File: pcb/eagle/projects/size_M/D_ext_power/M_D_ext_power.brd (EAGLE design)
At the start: 21 parts

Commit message: PCB M.1
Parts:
- added D.F1, D.F2: (no value), rcl:R0805
- added D.R2, D.R5: 5k1, rcl:R0603
- added D.R9: TERM_10K, hugo:THERM
- D.R3: value 12k -> 1k
- D.U1: value MCP -> MCP73833-AMI_UN; device !stavebnice03:SOT23-5 -> SamacSys_Parts:SOP50P490X110-10N
- D.U2: value TC -> LM3671_3.3
- moved D.U1 1.03 mm to (6.10, 13.7), turned to 0 degrees
- moved D.C7 0.59 mm to (9.74, 17.1)
- moved D.C6 0.54 mm to (5.21, 16.8), flipped to the top
- moved D.R7 0.18 mm to (14.7, 9.93)
- moved D.R4 0.14 mm to (8.43, 7.32)
- moved D.C4 0.09 mm to (8.39, 10.0)
- renumbered D.IC2 to D.U3
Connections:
- removed net N$11: D.R3.2, D.U1.5
- removed net N$12: D.J3.2, D.R7.1, D.T1.S, D.U2.VIN
- removed net N$13: D.C6.2, D.LIPOL.2, D.R8.2, D.U1.3, D.U3.7
- removed net N$8: D.R8.1, D.T1.D, D.U3.8
- removed net N$9: D.C4.2, D.J3.1, D.R4.2, D.T1.G, D.U1.4, U$1.A4B9, U$1.B4A9
- removed net VDD: D.C1.2, D.C7.2, D.D1.2, D.J3.3, D.L1.2, D.R1.1, D.U2.BP, D.U3.5
- new net 3V3F: D.F1.2, D.J3.3
- new net IN+: D.C6.2, D.LIPOL.2, D.R8.2, D.U1.10, D.U1.9, D.U3.8
- new net IN-: D.R8.1, D.T1.D, D.U3.7
- new net N$10: D.R9.2, D.U1.8
- new net N$4: D.R5.1, U$1.B5
- new net N$6: D.R2.1, U$1.A5
- new net N$7: D.R3.2, D.U1.6
- new net VBATF: D.F2.2, D.J3.2
- new net VCC: D.C1.2, D.C7.2, D.D1.2, D.F1.1, D.L1.2, D.R1.1, D.U2.BP, D.U3.5
- new net VMOT: D.F2.1, D.R7.1, D.T1.S, D.U2.VIN
- new net VUSB: D.C4.2, D.J3.1, D.R4.2, D.T1.G, D.U1.1, D.U1.2, U$1.A4B9, U$1.B4A9
- net GND: now also D.R2.2, D.R5.2, D.R9.1, D.U1.5; no longer D.U1.2
- net P4: now also D.U1.3; no longer D.U1.1
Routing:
- net VUSB: track 0.00 -> 35.7 mm, vias 0 -> 1
- net VDD: track 34.2 -> 0.00 mm, vias 1 -> 0
- net N$9: track 33.0 -> 0.00 mm, vias 1 -> 0
- net VCC: track 0.00 -> 30.9 mm, vias 0 -> 1
- net GND: track 99.6 -> 122.1 mm, vias 4 -> 6
- net N$13: track 16.0 -> 0.00 mm, vias 1 -> 0
- net N$12: track 14.8 -> 0.00 mm, vias 1 -> 0
- net IN+: track 0.00 -> 14.8 mm, vias 0 -> 2
- net VMOT: track 0.00 -> 14.6 mm, vias 0 -> 1
- net N$10: track 0.00 -> 13.7 mm, vias 0 -> 1
- net N$8: track 9.31 -> 0.00 mm, vias 1 -> 0
- net IN-: track 0.00 -> 8.86 mm, vias 0 -> 1
- net P4: track 14.6 -> 21.8 mm
- net 3V3F: track 0.00 -> 3.66 mm
- net VBATF: track 0.00 -> 3.21 mm
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- added copper zone on layer 16, net IN+
- added copper zone on layer 16, net VUSB

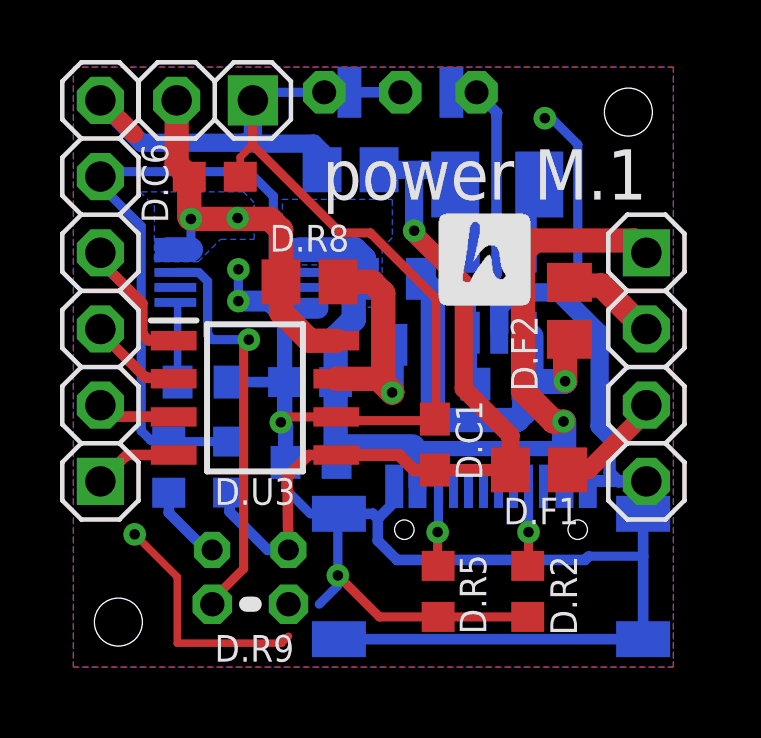
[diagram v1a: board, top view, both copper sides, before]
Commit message: repository structure reorganized (tiny-blocks moved to a separate directory) implemented tiny-power-block
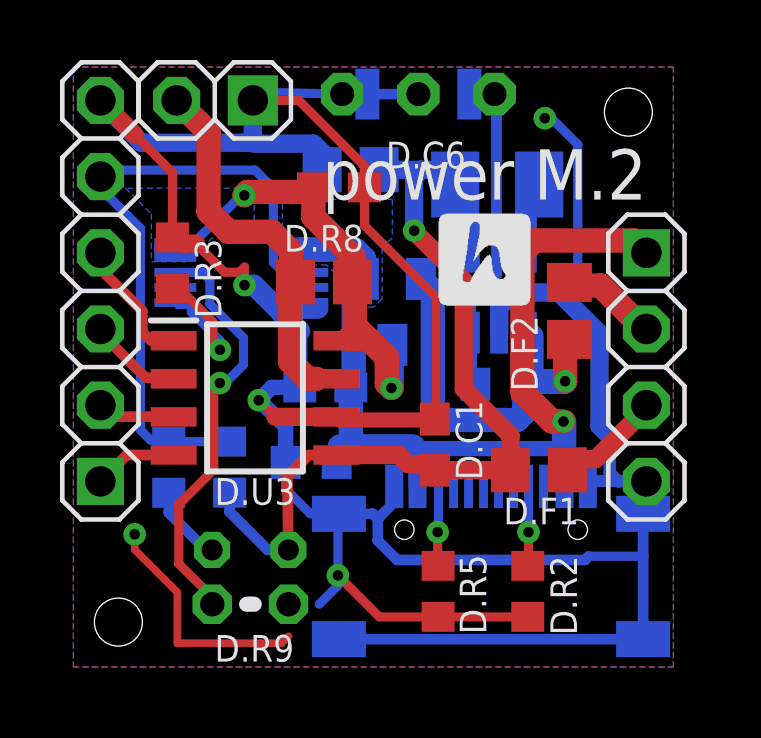
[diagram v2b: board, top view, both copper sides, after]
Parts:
- moved D.C6 4.16 mm to (9.35, 16.5)
- moved D.R3 4.10 mm to (3.80, 14.0), flipped to the top, turned to 270 degrees
- moved D.ON/OFF/RESET 0.60 mm to (12.0, 19.6)
- moved D.C4 0.54 mm to (8.90, 9.82)
- moved D.R8 0.48 mm to (8.85, 13.3)
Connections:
- net P0 renamed PA6
- net P1 renamed PA7
- net P4 renamed PA3
- net IN+: now also D.U3.7; no longer D.C6.2, D.U1.10, D.U1.9, D.U3.8
- net IN-: now also D.C6.2, D.U1.10, D.U1.9, D.U3.8; no longer D.U3.7
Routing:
- net IN-: track 8.86 -> 16.6 mm, vias 1 -> 2
- net GND: track 122.1 -> 127.3 mm, vias 6 -> 5
- net N$7: track 2.69 -> 5.29 mm, vias 0 -> 1
- net IN+: track 14.8 -> 13.0 mm, vias 2 -> 0
- added copper zone on layer 16, net IN-
- removed copper zone on layer 16, net IN+
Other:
- board text added: "power M.2"
- board text removed: "power M.1"

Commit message: closed PCB version M.2
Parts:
- D.R6: value 2k2 -> 330

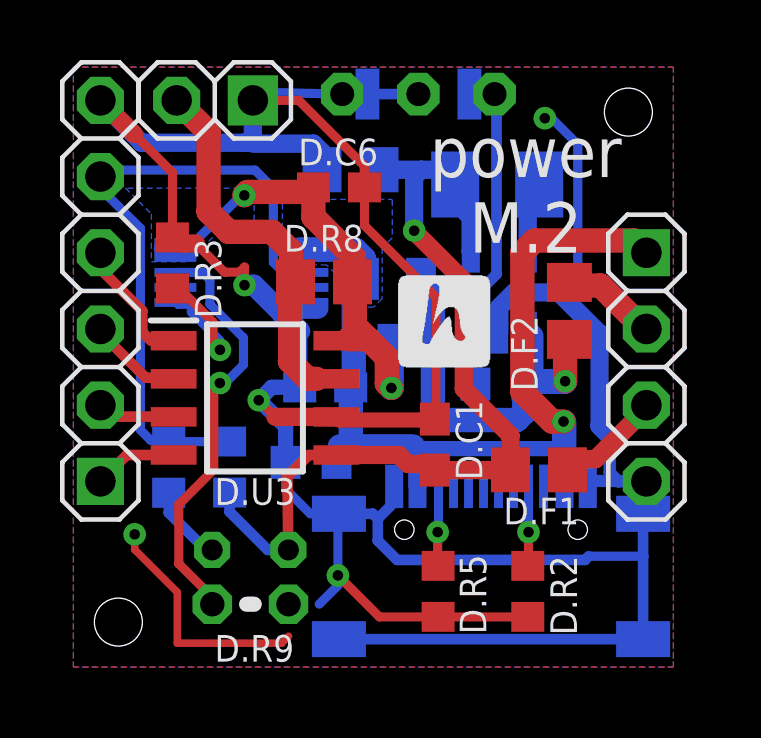
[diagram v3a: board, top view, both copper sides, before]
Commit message: updated power module to be handled charging correctly (LED + attiny pin)
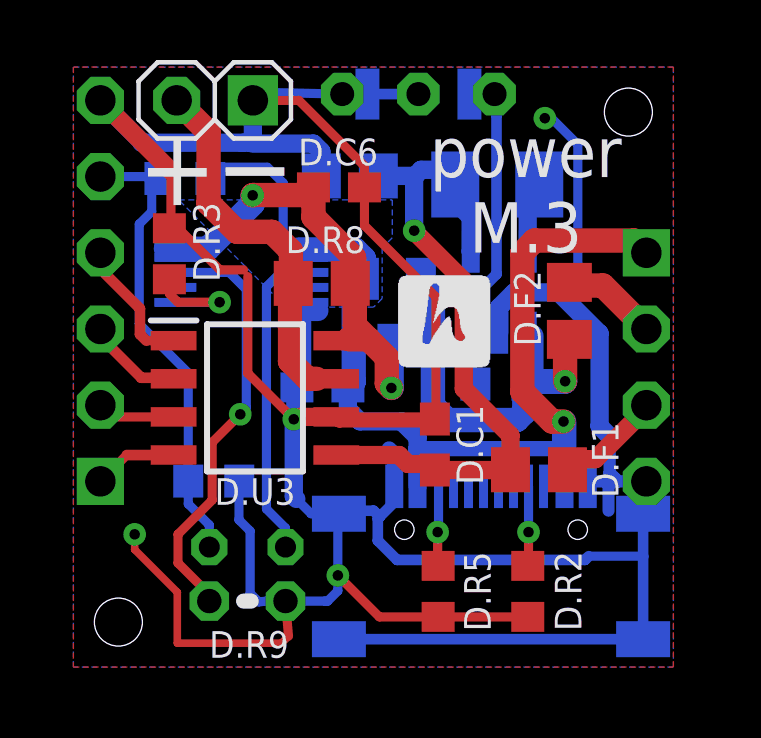
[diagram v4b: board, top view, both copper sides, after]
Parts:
- removed D.R4: 100k, rcl:R0603
- D.D1: value LED_1.8 -> LED_1.8_FLIPPED
- D.R1: value 100k -> 4k7
- D.R3: value 1k -> I=1/R (4k7 for 213mA, 2k2 for455mA )
- D.R6: value 330 -> 3k3
- moved D.R6 9.64 mm to (4.22, 16.8), turned to 180 degrees
- moved D.R1 0.71 mm to (5.18, 6.70), turned to 0 degrees
- moved D.R3 0.32 mm to (3.70, 14.3)
- moved D.C7 0.20 mm to (9.72, 16.9)
- moved D.R9 0.14 mm to (6.30, 2.70)
- moved D.D1 0.13 mm to (6.30, 4.10)
- moved D.C4 0.10 mm to (8.80, 9.82)
- moved D.R8 0.09 mm to (8.78, 13.3)
- flipped D.J2 to the bottom
- flipped D.J3 to the bottom
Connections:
- net GND: now also D.R1.1; no longer D.R4.1
- net N$3: now also D.J2.5, D.R1.2, D.R6.1; no longer D.R6.2
- net PA3: now also D.D1.2; no longer D.J2.5, D.R1.2, D.R6.1
- net VCC: no longer D.D1.2, D.R1.1
- net VUSB: now also D.R6.2; no longer D.R4.2
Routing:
- net N$3: track 3.32 -> 15.5 mm
- net PA3: track 22.0 -> 10.5 mm
- net GND: track 127.3 -> 136.9 mm, vias 5 -> 4
- net VCC: track 30.9 -> 23.2 mm
- net VUSB: track 35.7 -> 38.7 mm
- net N$7: track 5.29 -> 3.77 mm
- net IN-: track 16.6 -> 17.4 mm
- removed copper zone on layer 16, net IN-
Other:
- board text added: "power M.3"
- board text removed: "power M.2"

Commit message: added python code for power block refactoring i2c calls - run until complete doesn't work from async environment. improved active variable lot of small improvements adjusted another toold to be adjusted readme file tools/export splitted to tools/upload and tools/devel
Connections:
- removed net N$3: D.D1.1, D.J2.5, D.R1.2, D.R6.1
- new net STAT1: D.D1.2, D.U1.3
- net PA3: now also D.D1.1, D.J2.5, D.R1.2, D.R6.1; no longer D.D1.2, D.U1.3
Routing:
- net N$3: track 15.5 -> 0.00 mm
- net STAT1: track 0.00 -> 10.5 mm
- net PA3: track 10.5 -> 15.5 mm
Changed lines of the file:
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@@
 <grid distance="1" unitdist="mil" unit="mm" style="lines" multiple="1" display="yes" altdistance="0.1" altunitdist="mm" altunit="mm"/>
 <layers>
-<layer number="1" name="Top" color="4" fill="1" visible="no" active="yes"/>
-<layer number="16" name="Bottom" color="1" fill="1" visible="no" active="yes"/>
+<layer number="1" name="Top" color="4" fill="1" visible="yes" active="yes"/>
+<layer number="16" name="Bottom" color="1" fill="1" visible="yes" active="yes"/>
 <layer number="17" name="Pads" color="2" fill="1" visible="yes" active="yes"/>
 <layer number="18" name="Vias" color="2" fill="1" visible="yes" active="yes"/>
-<layer number="19" name="Unrouted" color="6" fill="1" visible="no" active="yes"/>
-<layer number="20" name="Dimension" color="24" fill="1" visible="no" active="yes"/>
+<layer number="19" name="Unrouted" color="6" fill="1" visible="yes" active="yes"/>
+<layer number="20" name="Dimension" color="24" fill="1" visible="yes" active="yes"/>
 <layer number="21" name="tPlace" color="23" fill="1" visible="yes" active="yes"/>
-<layer number="22" name="bPlace" color="47" fill="1" visible="no" active="yes"/>
+<layer number="22" name="bPlace" color="47" fill="1" visible="yes" active="yes"/>
 <layer number="23" name="tOrigins" color="15" fill="1" visible="yes" active="yes"/>
-<layer number="24" name="bOrigins" color="15" fill="1" visible="no" active="yes"/>
+<layer number="24" name="bOrigins" color="15" fill="1" visible="yes" active="yes"/>
 <layer number="25" name="tNames" color="7" fill="1" visible="yes" active="yes"/>
-<layer number="26" name="bNames" color="7" fill="1" visible="no" active="yes"/>
+<layer number="26" name="bNames" color="7" fill="1" visible="yes" active="yes"/>
 <layer number="27" name="tValues" color="7" fill="1" visible="no" active="yes"/>
 <layer number="28" name="bValues" color="7" fill="1" visible="no" active="yes"/>
-<layer number="29" name="tStop" color="7" fill="3" visible="yes" active="yes"/>
+<layer number="29" name="tStop" color="7" fill="3" visible="no" active="yes"/>
 <layer number="30" name="bStop" color="7" fill="6" visible="no" active="yes"/>
 <layer number="31" name="tCream" color="7" fill="4" visible="no" active="yes"/>
@@
 <layer number="37" name="tTest" color="7" fill="1" visible="no" active="yes"/>
 <layer number="38" name="bTest" color="7" fill="1" visible="no" active="yes"/>
-<layer number="39" name="tKeepout" color="4" fill="11" visible="no" active="yes"/>
-<layer number="40" name="bKeepout" color="1" fill="11" visible="no" active="yes"/>
-<layer number="41" name="tRestrict" color="4" fill="10" visible="no" active="yes"/>
-<layer number="42" name="bRestrict" color="1" fill="10" visible="no" active="yes"/>
+<layer number="39" name="tKeepout" color="4" fill="11" visible="yes" active="yes"/>
+<layer number="40" name="bKeepout" color="1" fill="11" visible="yes" active="yes"/>
+<layer number="41" name="tRestrict" color="4" fill="10" visible="yes" active="yes"/>
+<layer number="42" name="bRestrict" color="1" fill="10" visible="yes" active="yes"/>
 <layer number="43" name="vRestrict" color="2" fill="10" visible="no" active="yes"/>
 <layer number="44" name="Drills" color="7" fill="1" visible="no" active="yes"/>
@@
 <layer number="46" name="Milling" color="3" fill="1" visible="no" active="yes"/>
 <layer number="47" name="Measures" color="7" fill="1" visible="no" active="yes"/>
-<layer number="48" name="Document" color="49" fill="1" visible="yes" active="yes"/>
+<layer number="48" name="Document" color="49" fill="1" visible="no" active="yes"/>
 <layer number="49" name="Reference" color="7" fill="1" visible="no" active="yes"/>
 <layer number="50" name="dxf" color="7" fill="1" visible="no" active="no"/>
-<layer number="51" name="tDocu" color="7" fill="1" visible="no" active="yes"/>
-<layer number="52" name="bDocu" color="7" fill="1" visible="no" active="yes"/>
+<layer number="51" name="tDocu" color="7" fill="1" visible="yes" active="yes"/>
+<layer number="52" name="bDocu" color="7" fill="1" visible="yes" active="yes"/>
 <layer number="53" name="tGND_GNDA" color="7" fill="9" visible="no" active="no"/>
 <layer number="54" name="bGND_GNDA" color="1" fill="9" visible="no" active="no"/>
@@
 <wire x1="16.0304" y1="16.2018" x2="16.0304" y2="16.5862" width="0.6096" layer="16"/>
 </signal>
-<signal name="PA3">
+<signal name="STAT1">
 <contactref element="D.U1" pad="3"/>
 <contactref element="D.D1" pad="2"/>
@@
 <wire x1="15.060521875" y1="7.067184375" x2="15.06978125" y2="7.07644375" width="0.4064" layer="1"/>
 </signal>
-<signal name="N$3">
+<signal name="PA3">
 <contactref element="D.J2" pad="5"/>
 <contactref element="D.D1" pad="1"/>

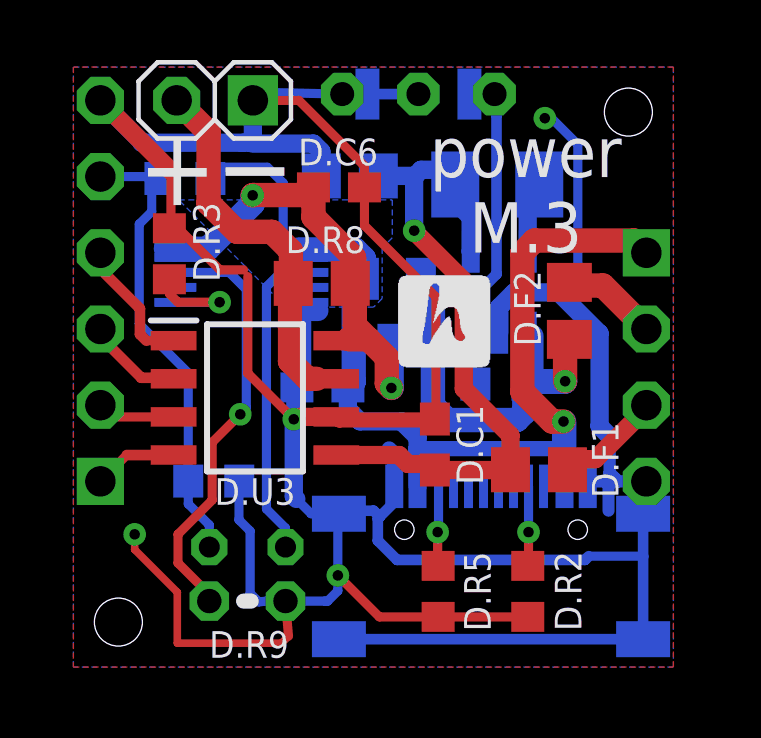
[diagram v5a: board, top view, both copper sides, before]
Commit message: button block + chassis + default i2c addresses
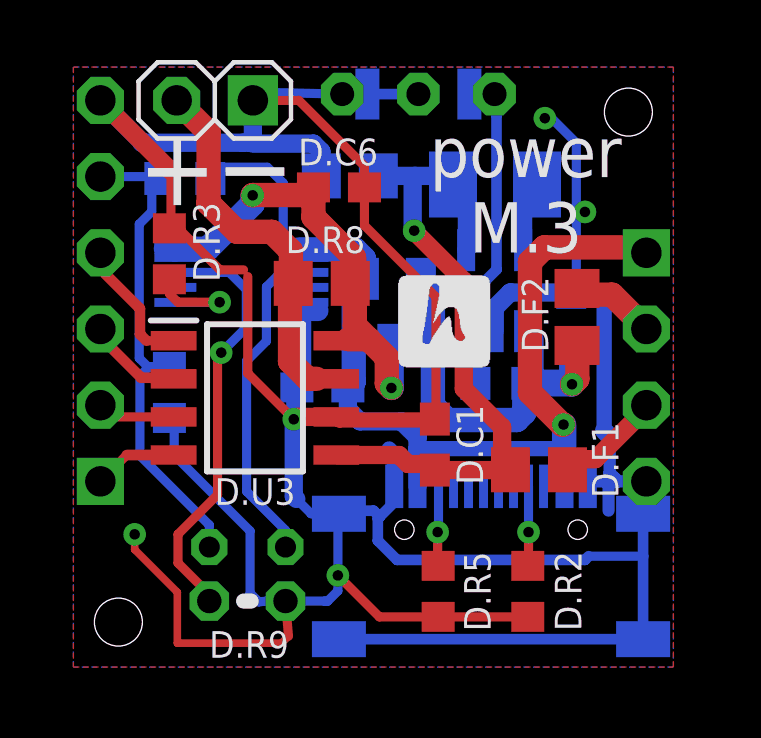
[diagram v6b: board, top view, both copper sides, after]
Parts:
- added D.C2: 4u7, rcl:C0603
- D.C7: value 22u -> 10u
- D.F1: value (none) -> 0.5A
- D.F2: value (none) -> 1.1A
- D.R7: value 100k -> 390k
- moved D.R1 3.31 mm to (3.70, 9.65), turned to 90 degrees
- moved D.F2 0.33 mm to (17.3, 12.2)
- moved D.U2 0.16 mm to (14.5, 13.0)
- moved D.L1 0.08 mm to (14.6, 16.6)
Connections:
- net GND: now also D.C2.1
- net VMOT: now also D.C2.2
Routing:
- net GND: track 136.9 -> 140.4 mm, vias 4 -> 5
- net VMOT: track 14.5 -> 16.6 mm
- net PA3: track 15.5 -> 17.2 mm
- net VUSB: track 38.7 -> 37.8 mm
- net STAT1: track 10.5 -> 11.0 mm
- removed copper zone on layer 16, net VUSB

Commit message: inverted logic of power switch to be left for off and right for on
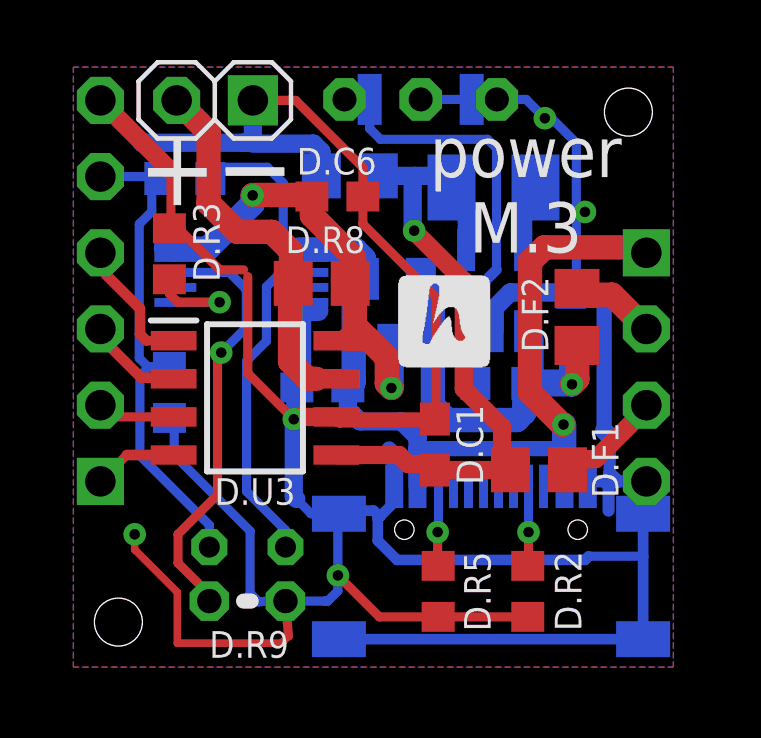
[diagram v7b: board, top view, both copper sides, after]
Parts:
- moved D.C6 0.31 mm to (9.30, 16.2)
- moved D.ON/OFF/RESET 0.19 mm to (12.1, 19.4)
- moved D.L1 0.11 mm to (14.5, 16.5)
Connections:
- net GND: now also D.ON/OFF/RESET.P$1, D.ON/OFF/RESET.P$4; no longer D.ON/OFF/RESET.P$3, D.ON/OFF/RESET.P$5
- net N$5: now also D.ON/OFF/RESET.P$3, D.ON/OFF/RESET.P$5; no longer D.ON/OFF/RESET.P$1, D.ON/OFF/RESET.P$4
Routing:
- net N$5: track 11.1 -> 13.9 mm
- net GND: track 140.4 -> 139.4 mm

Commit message: updated main board - added 5 to 3.3V regulator becaues one in CP is too weak updated power board - added shotky diode to FET to be sure it works as expected
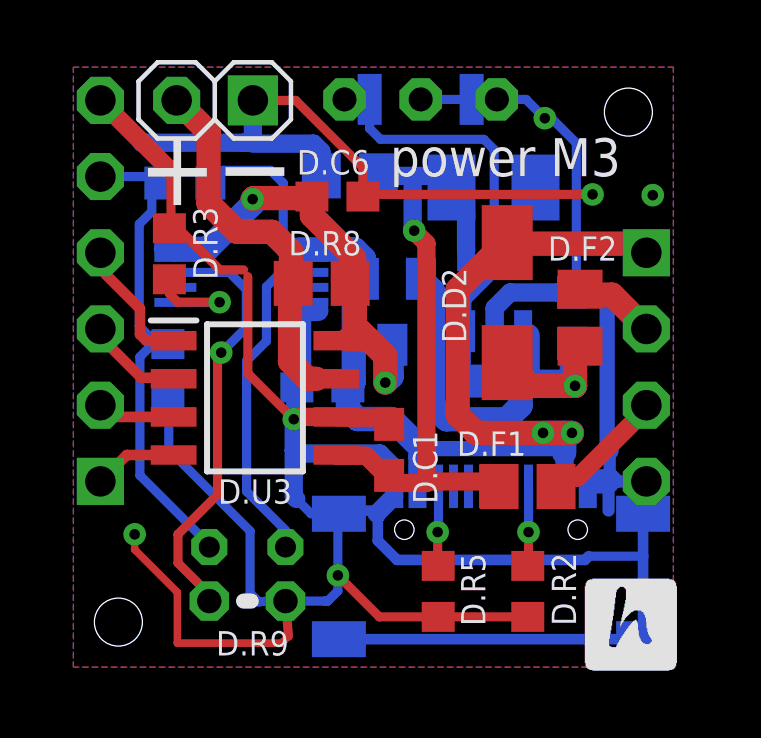
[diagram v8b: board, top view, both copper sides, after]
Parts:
- added D.D2: SHOTKY, hugo:SHOTKY
- D.T1: value FDV -> FDV304
- moved D.C1 1.53 mm to (11.0, 7.74)
- moved D.R1 0.76 mm to (3.65, 10.4)
- moved D.F1 0.68 mm to (15.6, 6.52)
- moved D.R6 0.15 mm to (4.22, 16.6)
- moved D.R7 0.13 mm to (14.6, 10.0)
- moved D.F2 0.10 mm to (17.4, 12.1)
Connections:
- net VMOT: now also D.D2.K
- net VUSB: now also D.D2.A
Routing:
- net VUSB: track 37.8 -> 43.9 mm, vias 1 -> 2
- net GND: track 139.4 -> 142.6 mm, vias 5 -> 6
- net VMOT: track 16.6 -> 19.4 mm
- net VCC: track 22.9 -> 22.1 mm
- net 3V3F: track 3.58 -> 4.21 mm
- net N$5: track 13.9 -> 14.5 mm
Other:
- board text added: "power M3"
- board text removed: "power M.3"
